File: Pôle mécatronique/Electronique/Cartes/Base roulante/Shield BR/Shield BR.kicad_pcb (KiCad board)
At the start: 2 copper layers, 66 x 61 mm, 40 parts, among them J1 Conn_01x04_Male, J2 Conn_01x04_Female, J3 Conn_01x04_Female, J4 Conn_01x04_Female, J5 Conn_01x04_Female, J5-CAN1 Conn_01x02_Female, SW1 SW_Push_SPDT, U1 R-78E5.0-0.5, U2 MCP2551-I-P

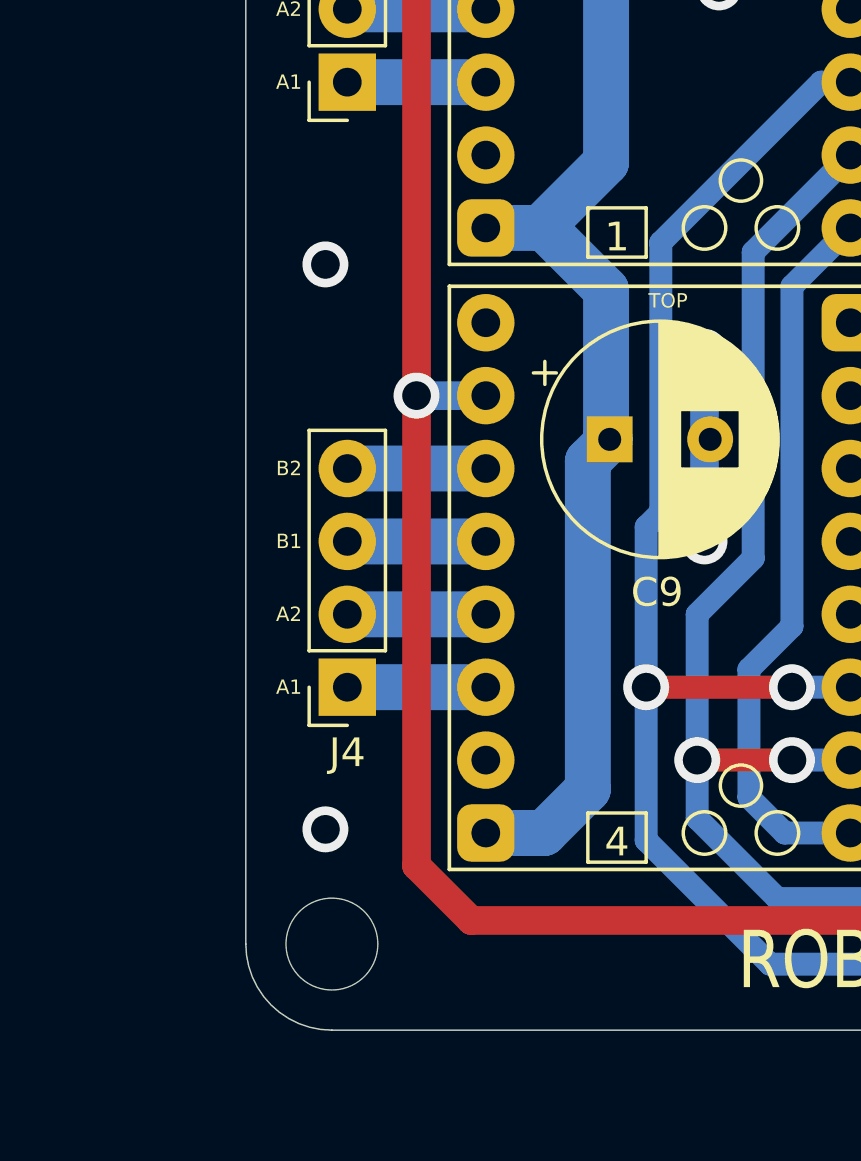
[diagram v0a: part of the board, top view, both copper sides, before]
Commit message: Ajout points de masse
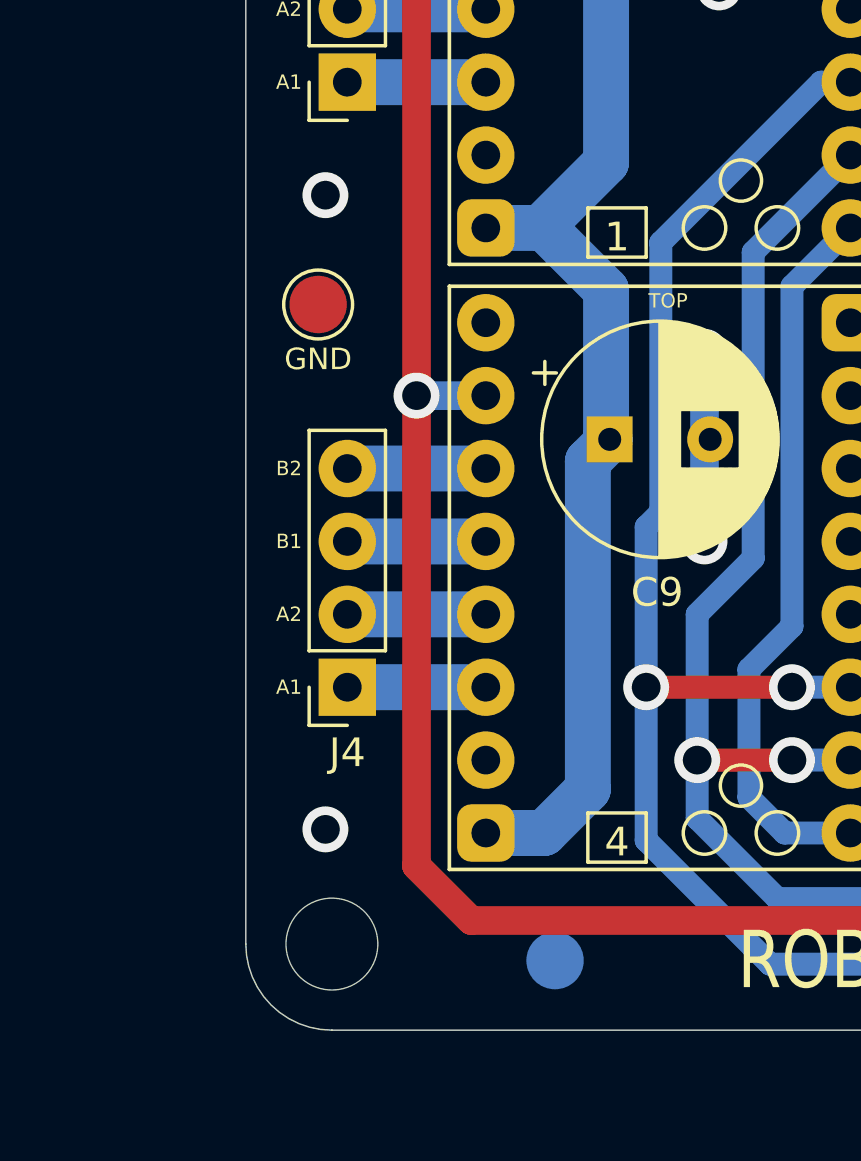
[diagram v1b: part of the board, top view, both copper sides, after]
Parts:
- added TP10: TestPoint, TestPoint:TestPoint_Pad_D2.0mm, B.Cu at (89.0, 122.3)
- added TP11: TestPoint, TestPoint:TestPoint_Pad_D2.0mm, F.Cu at (80.8, 99.4)
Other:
- board text added: "GND"
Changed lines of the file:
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@@
     )
+  )
+  (footprint "TestPoint:TestPoint_Pad_D2.0mm" (layer "F.Cu")
+    (at 80.7715 99.441)
+    (descr "SMD pad as test Point, diameter 2.0mm")
+    (tags "test point SMD pad")
+    (property "Sheetfile" "Shield BR.kicad_sch")
+    (property "Sheetname" "")
+    (attr exclude_from_pos_files)
+    (fp_text reference "TP11" (at 0 -1.998) (layer "F.SilkS") hide
+      (effects (font (size 1 1) (thickness 0.15)))
+    )
+    (fp_text value "TestPoint" (at 0 2.05) (layer "F.Fab")
+      (effects (font (size 1 1) (thickness 0.15)))
+    )
+    (fp_text user "${REFERENCE}" (at 0 -2) (layer "F.Fab")
+      (effects (font (size 1 1) (thickness 0.15)))
+    )
+    (fp_circle (center 0 0) (end 0 1.2) (layer "F.SilkS") (width 0.12) (fill none))
+    (fp_circle (center 0 0) (end 1.5 0) (layer "F.CrtYd") (width 0.05) (fill none))
+    (pad "1" smd circle locked (at 0 0) (size 2 2) (layers "F.Cu" "F.Mask")
+      (net 2 "GND") (pinfunction "1") (pintype "passive"))
   )
   (footprint "Capacitor_SMD:C_1206_3216Metric_Pad1.33x1.80mm_HandSolder" (layer "F.Cu")
@@
   )
   (footprint "TestPoint:TestPoint_Pad_D2.0mm" (layer "B.Cu")
+    (at 89.0265 122.301 180)
+    (descr "SMD pad as test Point, diameter 2.0mm")
+    (tags "test point SMD pad")
+    (property "Sheetfile" "Shield BR.kicad_sch")
+    (property "Sheetname" "")
+    (attr exclude_from_pos_files)
+    (fp_text reference "TP10" (at 0 1.998) (layer "B.SilkS") hide
+      (effects (font (size 1 1) (thickness 0.15)) (justify mirror))
+    )
+    (fp_text value "TestPoint" (at 0 -2.05) (layer "B.Fab")
+      (effects (font (size 1 1) (thickness 0.15)) (justify mirror))
+    )
+    (fp_text user "${REFERENCE}" (at 0 2) (layer "B.Fab")
+      (effects (font (size 1 1) (thickness 0.15)) (justify mirror))
+    )
+    (fp_circle (center 0 0) (end 0 -1.2) (layer "B.SilkS") (width 0.12) (fill none))
+    (fp_circle (center 0 0) (end 1.5 0) (layer "B.CrtYd") (width 0.05) (fill none))
+    (pad "1" smd circle locked (at 0 0 180) (size 2 2) (layers "B.Cu" "B.Mask")
+      (net 2 "GND") (pinfunction "1") (pintype "passive"))
+  )
+  (footprint "TestPoint:TestPoint_Pad_D2.0mm" (layer "B.Cu")
     (at 126.1105 68.199 180)
     (descr "SMD pad as test Point, diameter 2.0mm")
@@
     (effects (font (size 1 1) (thickness 0.15)) (justify mirror))
   )
+  (gr_text "GND\n" (at 86.3595 122.809) (layer "B.SilkS")
+    (effects (font (size 0.75 0.75) (thickness 0.15)) (justify mirror))
+  )
   (gr_text "CAN_Rx" (at 101.3455 108.966 90) (layer "B.SilkS")
     (effects (font (size 1 1) (thickness 0.15)) (justify right mirror))
@@
   (gr_text "1" (at 91.1855 97.0915) (layer "F.SilkS")
     (effects (font (size 1 1) (thickness 0.15)))
+  )
+  (gr_text "GND\n" (at 80.7715 101.346) (layer "F.SilkS")
+    (effects (font (size 0.75 0.75) (thickness 0.15)))
   )
   (gr_text "ON" (at 80.7715 72.136 90) (layer "F.SilkS")
@@
   (via (at 94.7415 88.392) (size 1.6) (drill 1) (layers "F.Cu" "B.Cu") (free) (net 2))
   (via (at 111.7595 65.532) (size 1.6) (drill 1) (layers "F.Cu" "B.Cu") (free) (net 2))
-  (via (at 81.0255 98.044) (size 1.6) (drill 1) (layers "F.Cu" "B.Cu") (free) (net 2))
+  (via (at 81.0255 95.631) (size 1.6) (drill 1) (layers "F.Cu" "B.Cu") (free) (net 2))
   (via (at 116.5855 118.364) (size 1.6) (drill 1) (layers "F.Cu" "B.Cu") (free) (net 2))
   (via (at 141.2235 97.79) (size 1.6) (drill 1) (layers "F.Cu" "B.Cu") (free) (net 2))
